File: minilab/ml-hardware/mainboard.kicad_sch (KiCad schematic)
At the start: 9 parts

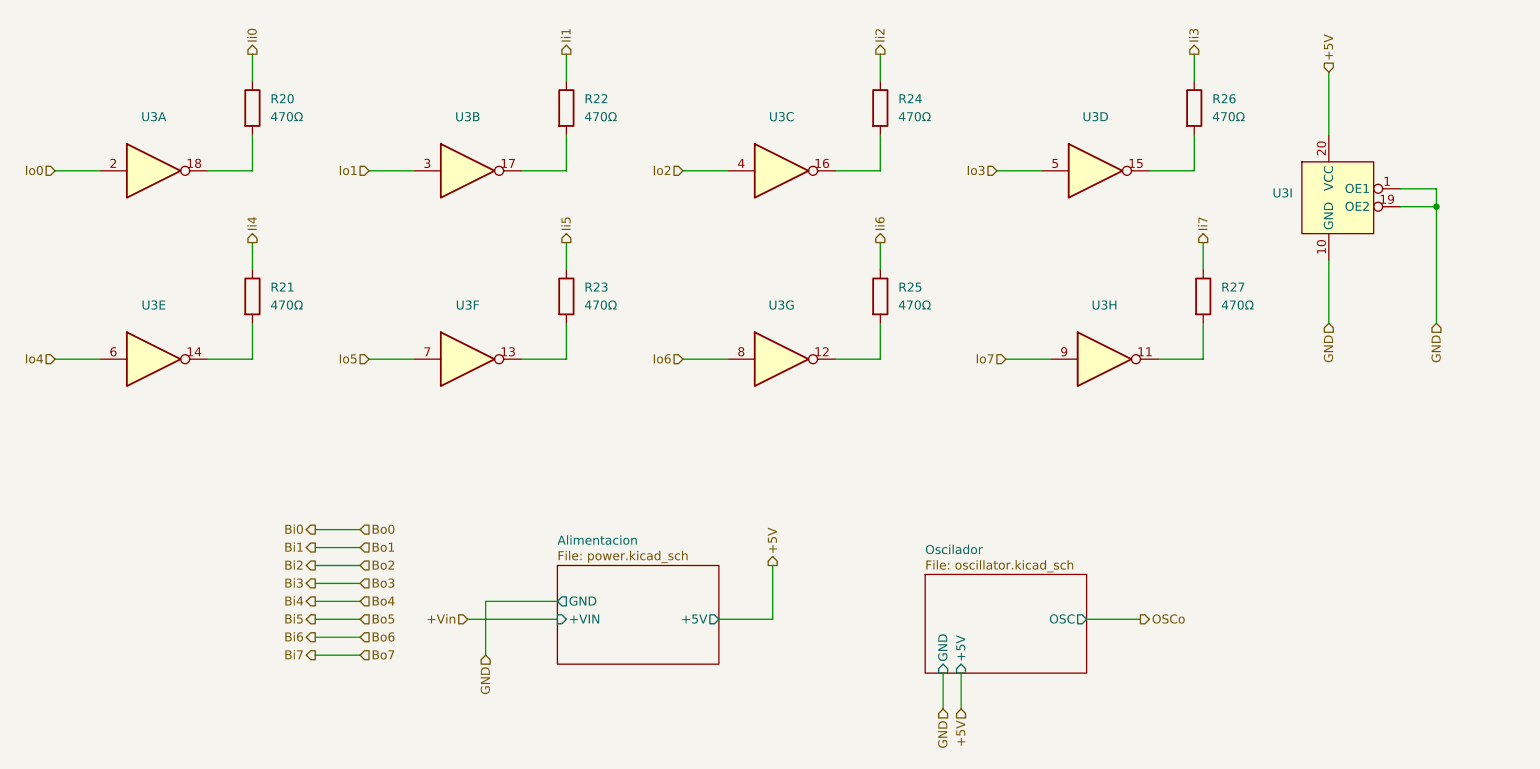
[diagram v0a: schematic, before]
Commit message: minilab: cambia jerarquia y agrega pcb
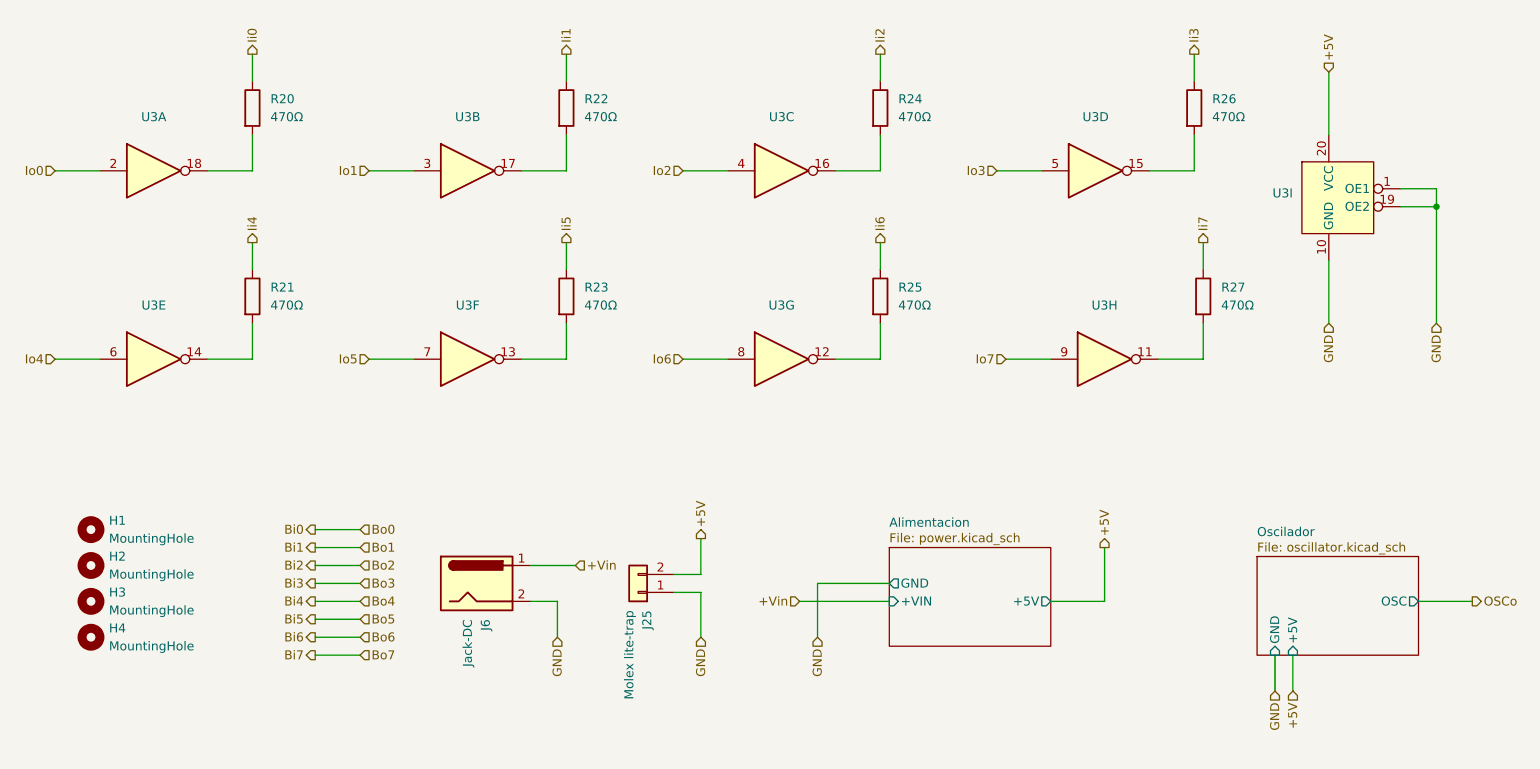
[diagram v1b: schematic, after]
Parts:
- added H1, H2, H3, H4: MountingHole, MountingHole:MountingHole_3.2mm_M3, symbol Mechanical:MountingHole
- added J25: Molex lite-trap, Extras:104238-0210, symbol Connector_Generic:Conn_01x02
- added J6: Jack-DC, Connector_BarrelJack:BarrelJack_Horizontal, symbol Connector:Jack-DC
- R20, R27: footprint Resistor_THT:R_Axial_DIN0204_L3.6mm_D1.6mm_P5.08mm_Horizontal -> Resistor_THT:R_Axial_DIN0204_L3.6mm_D1.6mm_P7.62mm_Horizontal
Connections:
- net +5V: now also J25.2 (Pin_2)
- net +Vin: now also J6.1
- net GND: now also J25.1 (Pin_1), J6.2

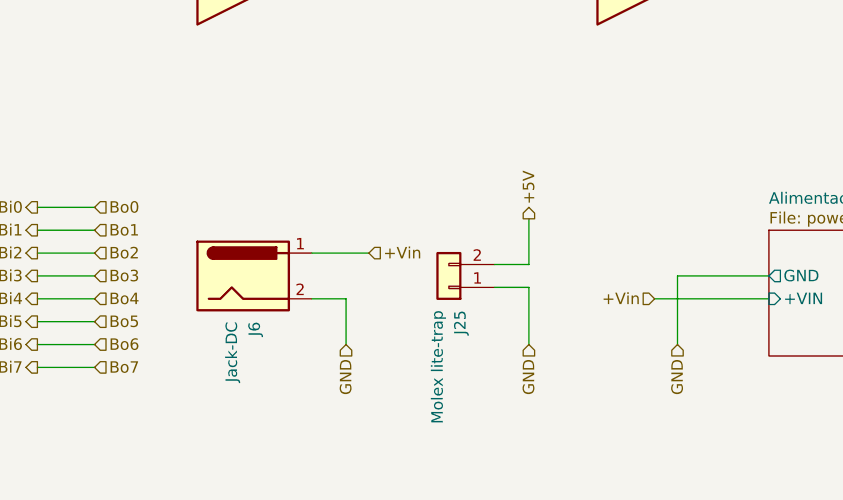
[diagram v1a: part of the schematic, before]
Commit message: minilab: Agrega 2da opc conectores y modelos 3d
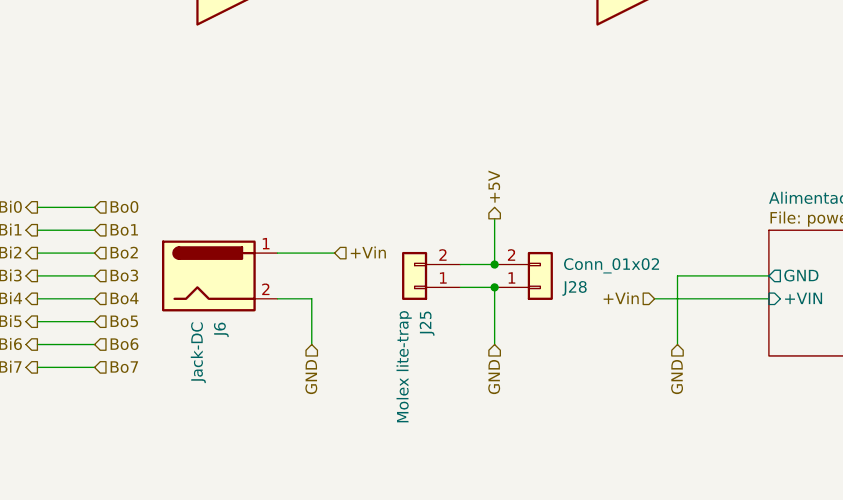
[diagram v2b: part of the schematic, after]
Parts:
- added J28: Conn_01x02, Connector_PinSocket_2.54mm:PinSocket_1x02_P2.54mm_Horizontal, symbol Connector_Generic:Conn_01x02
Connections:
- net +5V: now also J28.2 (Pin_2)
- net GND: now also J28.1 (Pin_1)
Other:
- moved on the sheet: J25, J6
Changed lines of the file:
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@@
+	)
+	(junction
+		(at 139.7 120.65)
+		(diameter 0)
+		(color 0 0 0 0)
 	)
 	(junction
@@
 		(color 0 0 0 0)
 	)
+	(junction
+		(at 139.7 118.11)
+		(diameter 0)
+		(color 0 0 0 0)
+	)
 	(wire
 		(pts
@@
 	(wire
 		(pts
-			(xy 143.51 113.03) (xy 143.51 118.11)
+			(xy 139.7 113.03) (xy 139.7 118.11)
 		)
 		(stroke
@@
 	(wire
 		(pts
-			(xy 139.7 120.65) (xy 143.51 120.65)
+			(xy 135.89 120.65) (xy 139.7 120.65)
 		)
 		(stroke
@@
 	(wire
 		(pts
-			(xy 123.19 121.92) (xy 123.19 127)
+			(xy 119.38 121.92) (xy 119.38 127)
 		)
 		(stroke
@@
 	(wire
 		(pts
-			(xy 119.38 116.84) (xy 125.73 116.84)
+			(xy 115.57 116.84) (xy 121.92 116.84)
 		)
 		(stroke
@@
 	(wire
 		(pts
-			(xy 119.38 121.92) (xy 123.19 121.92)
+			(xy 115.57 121.92) (xy 119.38 121.92)
 		)
 		(stroke
@@
 	(wire
 		(pts
-			(xy 143.51 120.65) (xy 143.51 127)
+			(xy 139.7 120.65) (xy 139.7 127)
 		)
 		(stroke
@@
 	(wire
 		(pts
-			(xy 143.51 118.11) (xy 139.7 118.11)
+			(xy 139.7 118.11) (xy 135.89 118.11)
 		)
 		(stroke
@@
 	(hierarchical_label "GND"
 		(shape input)
-		(at 123.19 127 270)
+		(at 119.38 127 270)
 		(effects
 			(font
@@
 	(hierarchical_label "+Vin"
 		(shape input)
-		(at 125.73 116.84 0)
+		(at 121.92 116.84 0)
 		(effects
 			(font
@@
 	(hierarchical_label "GND"
 		(shape input)
-		(at 143.51 127 270)
+		(at 139.7 127 270)
 		(effects
 			(font
@@
 	(hierarchical_label "+5V"
 		(shape output)
-		(at 143.51 113.03 90)
+		(at 139.7 113.03 90)
 		(effects
 			(font
@@
 	(symbol
 		(lib_id "Connector:Jack-DC")
-		(at 111.76 119.38 0)
+		(at 107.95 119.38 0)
 		(unit 1)
 		(exclude_from_sim no)
@@
 		(dnp no)
 		(property "Reference" "J6"
-			(at 113.0301 124.46 90)
+			(at 109.2201 124.46 90)
 			(effects
 				(font
@@
 		)
 		(property "Value" "Jack-DC"
-			(at 110.4901 124.46 90)
+			(at 106.6801 124.46 90)
 			(effects
 				(font
@@
 		)
 		(property "Footprint" "Connector_BarrelJack:BarrelJack_Horizontal"
-			(at 113.03 120.396 0)
+			(at 109.22 120.396 0)
 			(effects
 				(font
@@
 		)
 		(property "Datasheet" "~"
-			(at 113.03 120.396 0)
+			(at 109.22 120.396 0)
 			(effects
 				(font
@@
 		)
 		(property "Description" "DC Barrel Jack"
-			(at 111.76 119.38 0)
+			(at 107.95 119.38 0)
 			(effects
 				(font
@@
 	(symbol
 		(lib_id "Connector_Generic:Conn_01x02")
-		(at 134.62 120.65 180)
+		(at 130.81 120.65 180)
 		(unit 1)
 		(exclude_from_sim no)
@@
 		(dnp no)
 		(property "Reference" "J25"
-			(at 135.8901 123.19 90)
+			(at 132.0801 123.19 90)
 			(effects
 				(font
@@
 		)
 		(property "Value" "Molex lite-trap"
-			(at 133.3501 123.19 90)
+			(at 129.5401 123.19 90)
 			(effects
 				(font
@@
 		)
 		(property "Footprint" "Extras:104238-0210"
-			(at 134.62 120.65 0)
+			(at 130.81 120.65 0)
 			(effects
 				(font
@@
 		)
 		(property "Datasheet" "~"
-			(at 134.62 120.65 0)
+			(at 130.81 120.65 0)
 			(effects
 				(font
@@
 		)
 		(property "Description" "Generic connector, single row, 01x02, script generated (kicad-library-utils/schlib/autogen/connector/)"
-			(at 134.62 120.65 0)
+			(at 130.81 120.65 0)
 			(effects
 				(font
@@
 				)
 			)
+		)
+	)
+	(symbol
+		(lib_id "Connector_Generic:Conn_01x02")
+		(at 144.78 120.65 0)
+		(mirror x)
+		(unit 1)
+		(exclude_from_sim no)
+		(in_bom yes)
+		(on_board yes)
+		(dnp no)
+		(property "Reference" "J28"
+			(at 147.32 120.6501 0)
+			(effects
+				(font
+					(size 1.27 1.27)
+				)
+				(justify left)
+			)
+		)
+		(property "Value" "Conn_01x02"
+			(at 147.32 118.1101 0)
+			(effects
+				(font
+					(size 1.27 1.27)
+				)
+				(justify left)
+			)
+		)
+		(property "Footprint" "Connector_PinSocket_2.54mm:PinSocket_1x02_P2.54mm_Horizontal"
+			(at 144.78 120.65 0)
+			(effects
+				(font
+					(size 1.27 1.27)
+				)
+				(hide yes)
+			)
+		)
+		(property "Datasheet" "~"
+			(at 144.78 120.65 0)
+			(effects
+				(font
+					(size 1.27 1.27)
+				)
+				(hide yes)
+			)
+		)
+		(property "Description" "Generic connector, single row, 01x02, script generated (kicad-library-utils/schlib/autogen/connector/)"
+			(at 144.78 120.65 0)
+			(effects
+				(font
+					(size 1.27 1.27)
+				)
+				(hide yes)
+			)
+		)
+		(pin "2"
+		)
+		(pin "1"
+		)
+		(instances
+			(project "ml-hardware"
+				(path "/edb8a0df-1def-48df-b494-4a6b89ce8f9c/d397cdb8-1135-4612-aff9-bdf84d932419"
+					(reference "J28")
+					(unit 1)
+				)
+			)

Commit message: minilab: Corrige huella molex microfit y edge-*-02
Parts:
- J25: footprint Extras:104238-0210 -> Extras:Molex-Lite_trap
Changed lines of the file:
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@@
 			)
 		)
-		(property "Footprint" "Extras:104238-0210"
+		(property "Footprint" "Extras:Molex-Lite_trap"
 			(at 130.81 120.65 0)
 			(effects
